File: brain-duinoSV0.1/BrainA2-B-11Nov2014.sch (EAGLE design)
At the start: 40 parts, among them IC2 OP2177ARMZ, IC7 LT1761ES5-5

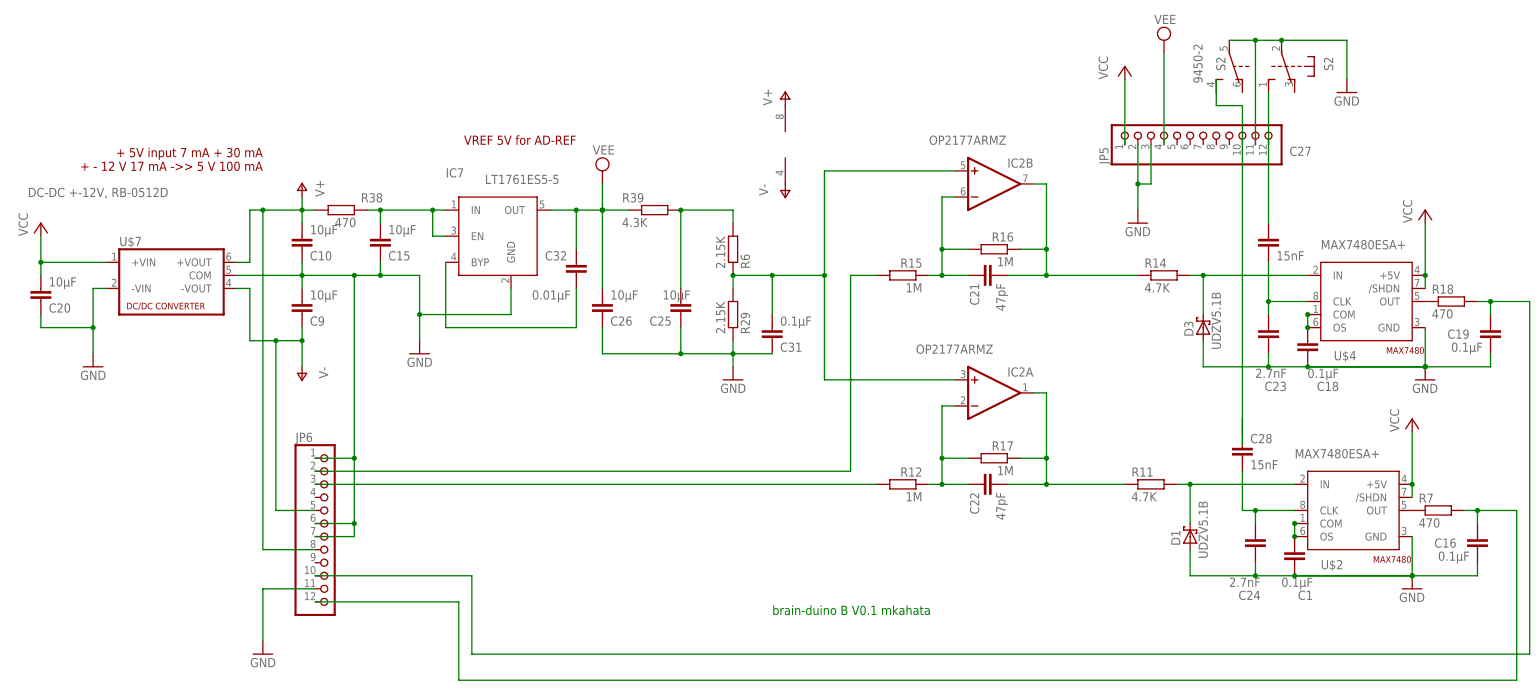
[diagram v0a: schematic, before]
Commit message: BrainA2-B: Getting rid of some schematic level ERC errors and warnings
Signed-off-by: Christoph Maier <cm.hardware.software.elsewhere@gmail.com>
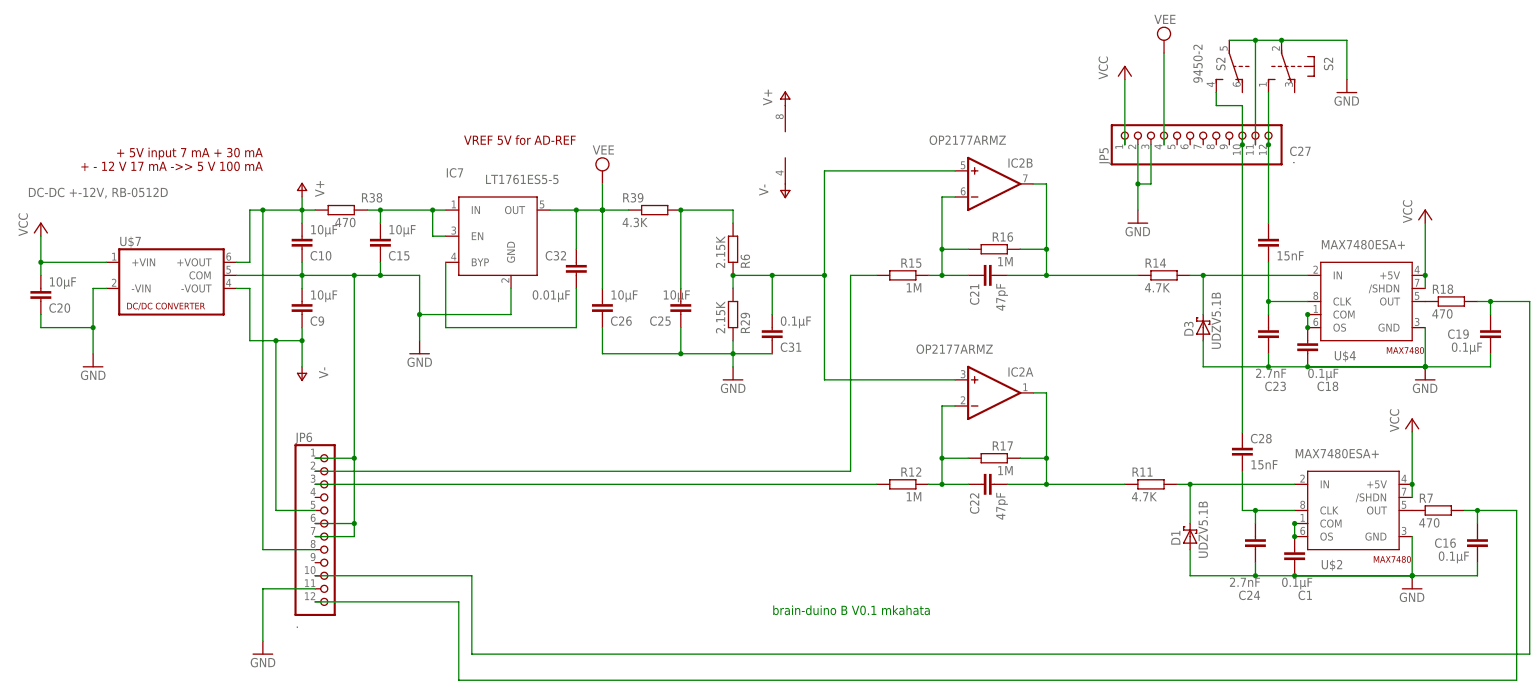
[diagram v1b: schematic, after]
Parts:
- JP5, JP6: value (none) -> .
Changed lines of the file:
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@@
 <?xml version="1.0" encoding="utf-8"?>
 <!DOCTYPE eagle SYSTEM "eagle.dtd">
-<eagle version="7.1.0">
+<eagle version="6.5.0">
 <drawing>
 <settings>
@@
 <part name="R29" library="rcl" deviceset="R-EU_" device="R0603" value="2.15K"/>
 <part name="R6" library="rcl" deviceset="R-EU_" device="R0603" value="2.15K"/>
-<part name="JP5" library="pinhead" deviceset="PINHD-1X12" device=""/>
-<part name="JP6" library="pinhead" deviceset="PINHD-1X12" device=""/>
+<part name="JP5" library="pinhead" deviceset="PINHD-1X12" device="" value="."/>
+<part name="JP6" library="pinhead" deviceset="PINHD-1X12" device="" value="."/>
 <part name="C1" library="rcl" deviceset="C-EU" device="C0603" value="0.1µF"/>
 <part name="R7" library="rcl" deviceset="R-EU_" device="R0603" value="470"/>
@@
 <wire x1="246.38" y1="167.64" x2="241.3" y2="167.64" width="0.1524" layer="91"/>
 <wire x1="241.3" y1="167.64" x2="241.3" y2="170.18" width="0.1524" layer="91"/>
-<wire x1="241.3" y1="170.18" x2="241.3" y2="172.72" width="0.1524" layer="91"/>
 <pinref part="JP5" gate="G$1" pin="10"/>
 <wire x1="246.38" y1="167.64" x2="246.38" y2="160.02" width="0.1524" layer="91"/>
 <pinref part="C28" gate="G$1" pin="1"/>
-<wire x1="246.38" y1="104.14" x2="246.38" y2="106.68" width="0.1524" layer="91"/>
-<wire x1="246.38" y1="104.14" x2="246.38" y2="101.6" width="0.1524" layer="91"/>
 <wire x1="246.38" y1="160.02" x2="246.38" y2="104.14" width="0.1524" layer="91"/>
+<junction x="246.38" y="160.02"/>
 </segment>
 </net>
@@
 <pinref part="S2" gate="1" pin="S"/>
 <wire x1="251.46" y1="170.18" x2="251.46" y2="160.02" width="0.1524" layer="91"/>
-</segment>
-</net>
+<junction x="251.46" y="160.02"/>
+</segment>
+</net>

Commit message: Rename U$2->IC10 U$4->IC11 U$7->IC12
Signed-off-by: Christoph Maier <cm.hardware.software.elsewhere@gmail.com>
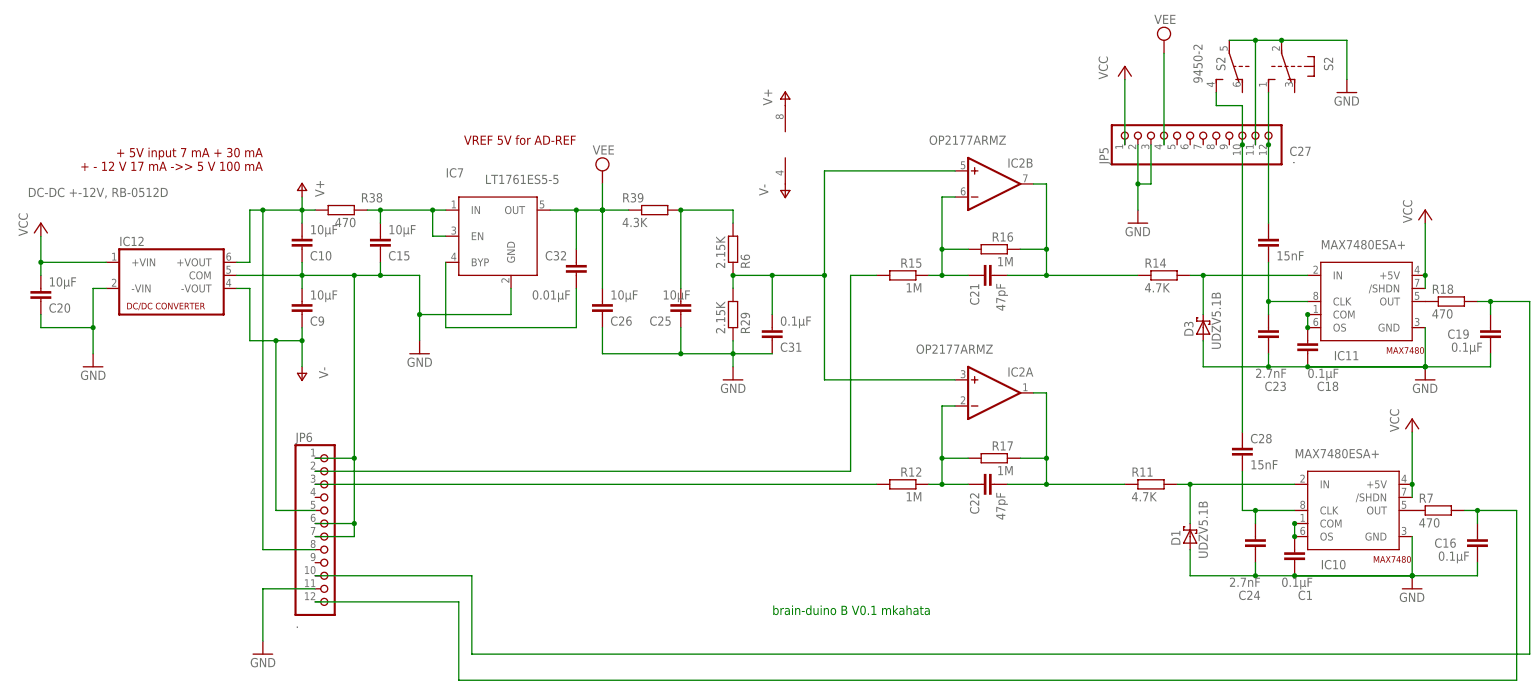
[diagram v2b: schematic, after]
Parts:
- renumbered U$2 to IC10, U$4 to IC11, U$7 to IC12
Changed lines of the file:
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@@
 <part name="R18" library="rcl" deviceset="R-EU_" device="R0603" value="470"/>
 <part name="C19" library="rcl" deviceset="C-EU" device="C0603" value="0.1µF"/>
-<part name="U$4" library="MKH" deviceset="MAX7480" device="" value="MAX7480ESA+"/>
+<part name="IC11" library="MKH" deviceset="MAX7480" device="" value="MAX7480ESA+"/>
 <part name="GND12" library="supply1" deviceset="GND" device=""/>
 <part name="R14" library="rcl" deviceset="R-EU_" device="R0603" value="4.7K"/>
@@
 <part name="C10" library="rcl" deviceset="C-EU" device="C0603" value="10µF"/>
 <part name="GND7" library="supply1" deviceset="GND" device=""/>
-<part name="U$7" library="MKH" deviceset="RB-0515D" device="" value="DC-DC +-12V, RB-0512D"/>
+<part name="IC12" library="MKH" deviceset="RB-0515D" device="" value="DC-DC +-12V, RB-0512D"/>
 <part name="C20" library="rcl" deviceset="C-EU" device="C0603" value="10µF"/>
 <part name="GND17" library="supply1" deviceset="GND" device=""/>
@@
 <part name="R7" library="rcl" deviceset="R-EU_" device="R0603" value="470"/>
 <part name="C16" library="rcl" deviceset="C-EU" device="C0603" value="0.1µF"/>
-<part name="U$2" library="MKH" deviceset="MAX7480" device="" value="MAX7480ESA+"/>
+<part name="IC10" library="MKH" deviceset="MAX7480" device="" value="MAX7480ESA+"/>
 <part name="GND1" library="supply1" deviceset="GND" device=""/>
 <part name="R11" library="rcl" deviceset="R-EU_" device="R0603" value="4.7K"/>
@@
 <attribute name="VALUE" x="293.116" y="121.539" size="1.778" layer="96" rot="R180"/>
 </instance>
-<instance part="U$4" gate="G$1" x="271.78" y="129.54" smashed="yes">
+<instance part="IC11" gate="G$1" x="271.78" y="129.54" smashed="yes">
 <attribute name="NAME" x="264.16" y="118.11" size="1.778" layer="95"/>
 <attribute name="VALUE" x="261.62" y="139.7" size="1.778" layer="96"/>
@@
 <instance part="C10" gate="G$1" x="63.5" y="139.7" rot="MR180"/>
 <instance part="GND7" gate="1" x="86.36" y="119.38" rot="MR0"/>
-<instance part="U$7" gate="G$1" x="38.1" y="132.08" smashed="yes">
+<instance part="IC12" gate="G$1" x="38.1" y="132.08" smashed="yes">
 <attribute name="NAME" x="27.94" y="140.335" size="1.778" layer="95"/>
 <attribute name="VALUE" x="10.16" y="149.86" size="1.778" layer="96"/>
@@
 <attribute name="VALUE" x="290.576" y="80.899" size="1.778" layer="96" rot="R180"/>
 </instance>
-<instance part="U$2" gate="G$1" x="269.24" y="88.9" smashed="yes">
+<instance part="IC10" gate="G$1" x="269.24" y="88.9" smashed="yes">
 <attribute name="NAME" x="261.62" y="77.47" size="1.778" layer="95"/>
 <attribute name="VALUE" x="256.54" y="99.06" size="1.778" layer="96"/>
@@
 <segment>
 <pinref part="C19" gate="G$1" pin="1"/>
-<pinref part="U$4" gate="G$1" pin="GND"/>
+<pinref part="IC11" gate="G$1" pin="GND"/>
 <wire x1="281.94" y1="116.84" x2="294.64" y2="116.84" width="0.1524" layer="91"/>
 <wire x1="294.64" y1="116.84" x2="294.64" y2="119.38" width="0.1524" layer="91"/>
@@
 <wire x1="104.14" y1="127" x2="86.36" y2="127" width="0.1524" layer="91"/>
 <junction x="86.36" y="127"/>
-<pinref part="U$7" gate="G$1" pin="COM"/>
+<pinref part="IC12" gate="G$1" pin="COM"/>
 <wire x1="78.74" y1="134.62" x2="73.66" y2="134.62" width="0.1524" layer="91"/>
 <pinref part="C10" gate="G$1" pin="1"/>
@@
 </segment>
 <segment>
-<pinref part="U$7" gate="G$1" pin="-VIN"/>
+<pinref part="IC12" gate="G$1" pin="-VIN"/>
 <wire x1="25.4" y1="132.08" x2="22.86" y2="132.08" width="0.1524" layer="91"/>
 <wire x1="22.86" y1="132.08" x2="22.86" y2="124.46" width="0.1524" layer="91"/>
@@
 <segment>
 <pinref part="C16" gate="G$1" pin="1"/>
-<pinref part="U$2" gate="G$1" pin="GND"/>
+<pinref part="IC10" gate="G$1" pin="GND"/>
 <wire x1="279.4" y1="76.2" x2="292.1" y2="76.2" width="0.1524" layer="91"/>
 <wire x1="292.1" y1="76.2" x2="292.1" y2="78.74" width="0.1524" layer="91"/>
@@
 <pinref part="C10" gate="G$1" pin="2"/>
 <wire x1="63.5" y1="149.86" x2="63.5" y2="147.32" width="0.1524" layer="91"/>
-<pinref part="U$7" gate="G$1" pin="+VOUT"/>
+<pinref part="IC12" gate="G$1" pin="+VOUT"/>
 <wire x1="63.5" y1="147.32" x2="63.5" y2="144.78" width="0.1524" layer="91"/>
 <wire x1="50.8" y1="137.16" x2="53.34" y2="137.16" width="0.1524" layer="91"/>
@@
 <wire x1="63.5" y1="116.84" x2="63.5" y2="121.92" width="0.1524" layer="91"/>
 <wire x1="63.5" y1="121.92" x2="58.42" y2="121.92" width="0.1524" layer="91"/>
-<pinref part="U$7" gate="G$1" pin="-VOUT"/>
+<pinref part="IC12" gate="G$1" pin="-VOUT"/>
 <wire x1="58.42" y1="121.92" x2="53.34" y2="121.92" width="0.1524" layer="91"/>
 <wire x1="50.8" y1="132.08" x2="53.34" y2="132.08" width="0.1524" layer="91"/>
@@
 <wire x1="259.08" y1="124.46" x2="259.08" y2="127" width="0.1524" layer="91"/>
 <pinref part="C18" gate="G$1" pin="2"/>
-<pinref part="U$4" gate="G$1" pin="OS"/>
+<pinref part="IC11" gate="G$1" pin="OS"/>
 <junction x="259.08" y="124.46"/>
-<pinref part="U$4" gate="G$1" pin="COM"/>
+<pinref part="IC11" gate="G$1" pin="COM"/>
 <junction x="259.08" y="127"/>
 </segment>
@@
 <segment>
 <pinref part="R18" gate="G$1" pin="1"/>
-<pinref part="U$4" gate="G$1" pin="OUT"/>
+<pinref part="IC11" gate="G$1" pin="OUT"/>
 </segment>
 </net>
 <net name="N$11" class="0">
 <segment>
-<pinref part="U$4" gate="G$1" pin="IN"/>
+<pinref part="IC11" gate="G$1" pin="IN"/>
 <pinref part="D3" gate="G$1" pin="C"/>
 <wire x1="238.76" y1="134.62" x2="259.08" y2="134.62" width="0.1524" layer="91"/>
@@
 <net name="VCC" class="0">
 <segment>
-<pinref part="U$4" gate="G$1" pin="+5V"/>
+<pinref part="IC11" gate="G$1" pin="+5V"/>
 <wire x1="281.94" y1="132.08" x2="281.94" y2="134.62" width="0.1524" layer="91"/>
-<pinref part="U$4" gate="G$1" pin="/SHDN"/>
+<pinref part="IC11" gate="G$1" pin="/SHDN"/>
 <wire x1="281.94" y1="134.62" x2="281.94" y2="144.78" width="0.1524" layer="91"/>
 <junction x="281.94" y="134.62"/>
@@
 </segment>
 <segment>
-<pinref part="U$2" gate="G$1" pin="+5V"/>
+<pinref part="IC10" gate="G$1" pin="+5V"/>
 <wire x1="279.4" y1="91.44" x2="279.4" y2="93.98" width="0.1524" layer="91"/>
-<pinref part="U$2" gate="G$1" pin="/SHDN"/>
+<pinref part="IC10" gate="G$1" pin="/SHDN"/>
 <wire x1="279.4" y1="93.98" x2="279.4" y2="104.14" width="0.1524" layer="91"/>
 <junction x="279.4" y="93.98"/>
@@
 <pinref part="C20" gate="G$1" pin="2"/>
 <wire x1="25.4" y1="137.16" x2="12.7" y2="137.16" width="0.1524" layer="91"/>
-<pinref part="U$7" gate="G$1" pin="+VIN"/>
+<pinref part="IC12" gate="G$1" pin="+VIN"/>
 <pinref part="P+6" gate="VCC" pin="VCC"/>
 <wire x1="12.7" y1="134.62" x2="12.7" y2="137.16" width="0.1524" layer="91"/>
@@
 <net name="N$91" class="0">
 <segment>
-<pinref part="U$4" gate="G$1" pin="CLK"/>
+<pinref part="IC11" gate="G$1" pin="CLK"/>
 <wire x1="251.46" y1="137.16" x2="251.46" y2="129.54" width="0.1524" layer="91"/>
 <wire x1="251.46" y1="129.54" x2="259.08" y2="129.54" width="0.1524" layer="91"/>
@@
 <wire x1="256.54" y1="83.82" x2="256.54" y2="86.36" width="0.1524" layer="91"/>
 <pinref part="C1" gate="G$1" pin="2"/>
-<pinref part="U$2" gate="G$1" pin="OS"/>
+<pinref part="IC10" gate="G$1" pin="OS"/>
 <junction x="256.54" y="83.82"/>
-<pinref part="U$2" gate="G$1" pin="COM"/>
+<pinref part="IC10" gate="G$1" pin="COM"/>
 <junction x="256.54" y="86.36"/>
 </segment>
@@
 <segment>
 <pinref part="R7" gate="G$1" pin="1"/>
-<pinref part="U$2" gate="G$1" pin="OUT"/>
+<pinref part="IC10" gate="G$1" pin="OUT"/>
 </segment>
 </net>
 <net name="N$14" class="0">
 <segment>
-<pinref part="U$2" gate="G$1" pin="IN"/>
+<pinref part="IC10" gate="G$1" pin="IN"/>
 <wire x1="233.68" y1="93.98" x2="236.22" y2="93.98" width="0.1524" layer="91"/>
 <pinref part="D1" gate="G$1" pin="C"/>
@@
 <net name="N$15" class="0">
 <segment>
-<pinref part="U$2" gate="G$1" pin="CLK"/>
+<pinref part="IC10" gate="G$1" pin="CLK"/>
 <wire x1="246.38" y1="88.9" x2="248.92" y2="88.9" width="0.1524" layer="91"/>
 <wire x1="248.92" y1="88.9" x2="256.54" y2="88.9" width="0.1524" layer="91"/>
